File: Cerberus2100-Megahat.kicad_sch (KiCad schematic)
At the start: 12 parts, among them J1 Power, J10 Cerberus 5V input, J2 PWM, J3 Analog, J4 PWM, J5 Analog, J6 Communication, J7 Digital, J8 Conn_02x20_Odd_Even, J9 Reset disable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

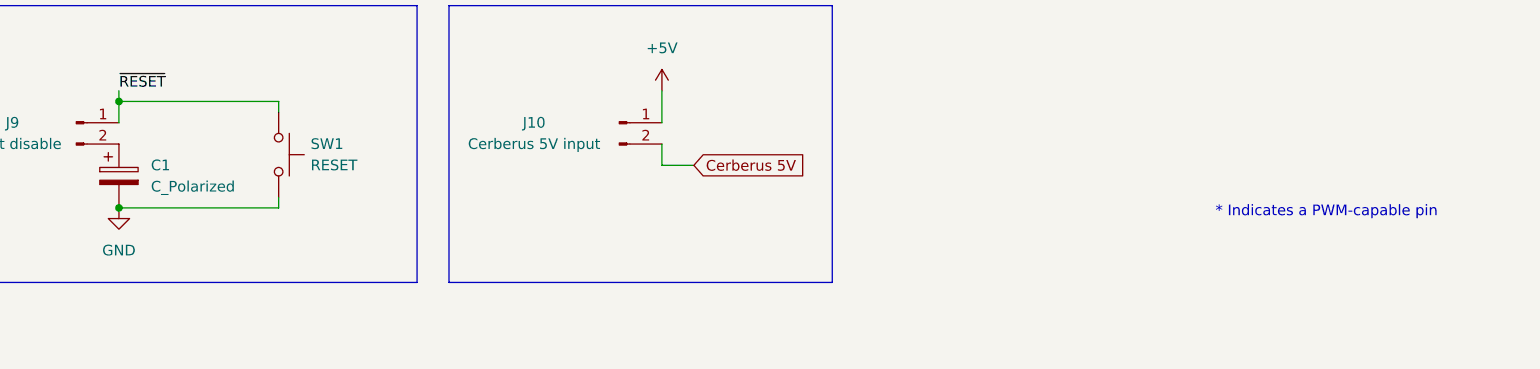
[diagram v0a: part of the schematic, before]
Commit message: Picture and Schema in PDF added
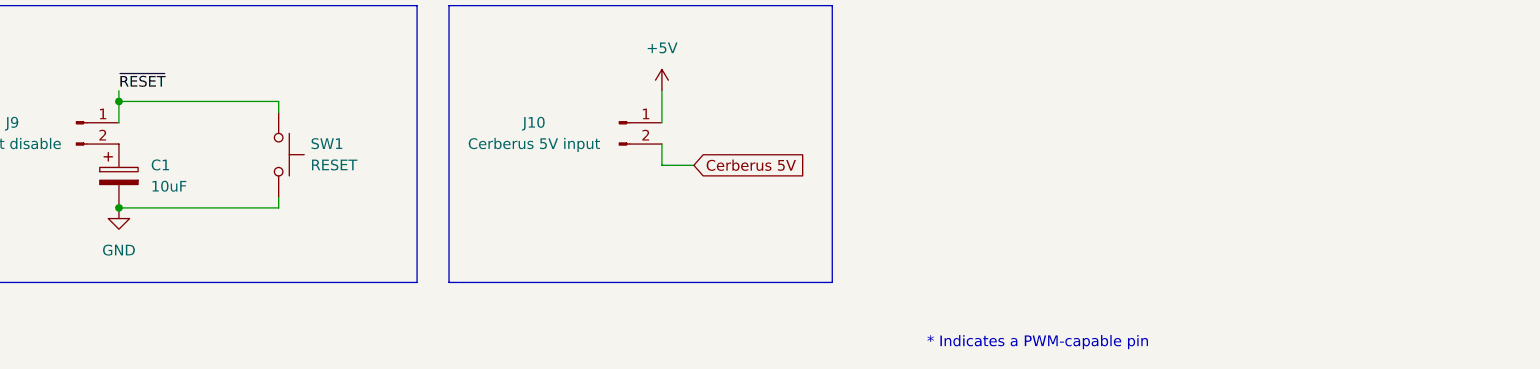
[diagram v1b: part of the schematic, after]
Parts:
- C1: value C_Polarized -> 10uF
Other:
- company: (none) -> Jeroen Venema
- title: (none) -> Cerberus 2100 MEGA Hat
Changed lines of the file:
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@@
   (paper "A4")
   (title_block
-    (date "mar. 31 mars 2015")
+    (title "Cerberus 2100 MEGA Hat")
+    (date "2024-02-09")
+    (rev "1.0")
+    (company "Jeroen Venema")
   )
   (junction (at 127 96.52) (diameter 0) (color 0 0 0 0)
@@
     (fill (type none))
   )
-  (text "* Indicates a PWM-capable pin" (at 177.8 180.34 0)
+  (text "* Indicates a PWM-capable pin" (at 143.383 195.961 0)
     (effects (font (size 1.27 1.27)) (justify left bottom))
   )
@@
       (effects (font (size 1.27 1.27)) (justify left))
     )
-    (property "Value" "C_Polarized" (at 50.8 176.53 0)
+    (property "Value" "10uF" (at 50.8 176.53 0)
       (effects (font (size 1.27 1.27)) (justify left))
     )
